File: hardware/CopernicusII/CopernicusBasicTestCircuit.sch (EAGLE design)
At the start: 6 parts, among them M1 COPERNICUS_II_MODULE

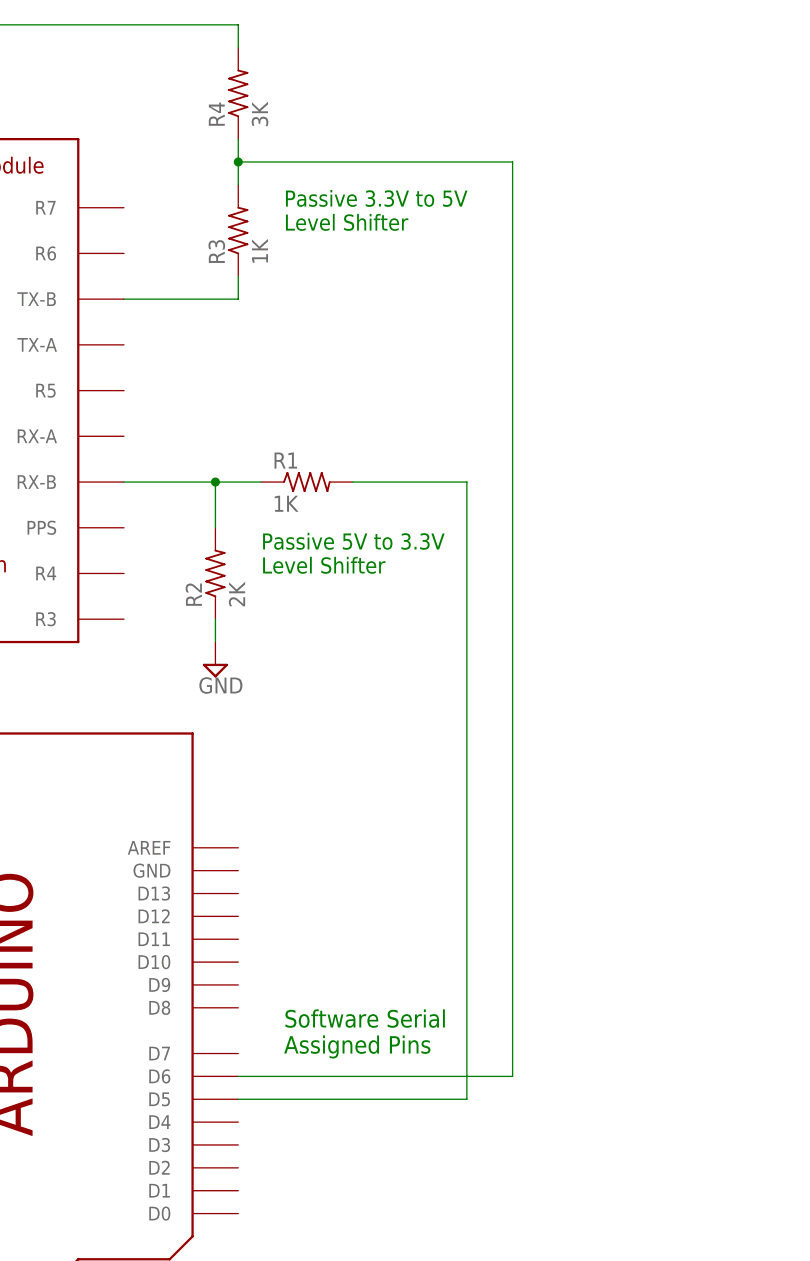
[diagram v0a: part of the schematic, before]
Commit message: Faster I/O with AltSoftSerial;Improved baud rate finding bug
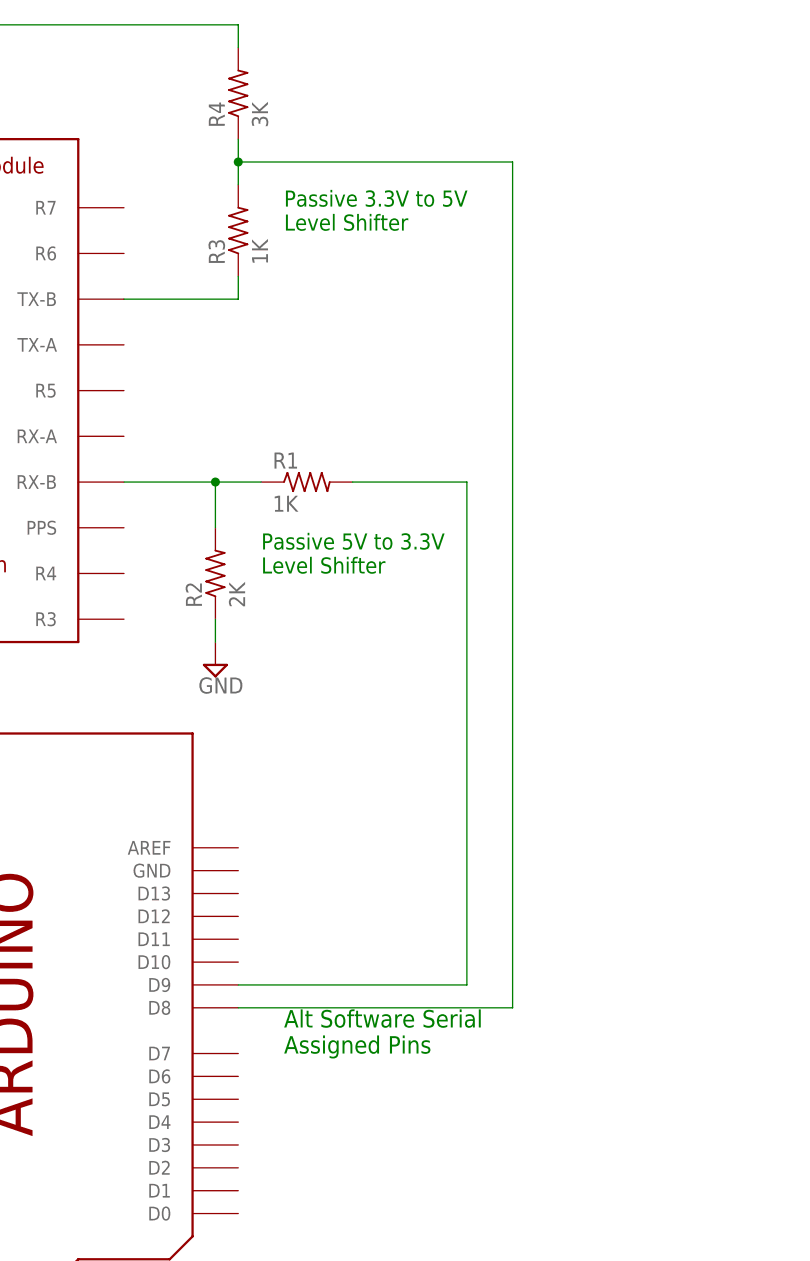
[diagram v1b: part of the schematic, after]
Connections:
- net N$2: now also U$1.D8; no longer U$1.D6
- net N$4: now also U$1.D9; no longer U$1.D5
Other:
- note added: "Alt Software Serial Assigned Pins"
- note removed: "Software Serial Assigned Pins"
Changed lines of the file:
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@@
 <plain>
 <text x="38.1" y="127" size="3.81" layer="91">Trimble Copernicus II Sparkfun Module Basic Test Circuit</text>
-<text x="144.78" y="7.62" size="1.9304" layer="91">Software Serial
+<text x="144.78" y="7.62" size="1.9304" layer="91">Alt Software Serial
 Assigned Pins</text>
 <text x="43.18" y="-12.7" size="1.778" layer="91">Rev 2.0.0
@@
 <pinref part="R1" gate="G$1" pin="2"/>
 <wire x1="165.1" y1="71.12" x2="152.4" y2="71.12" width="0.1524" layer="91"/>
-<wire x1="165.1" y1="71.12" x2="165.1" y2="2.54" width="0.1524" layer="91"/>
-<pinref part="U$1" gate="G$1" pin="D5"/>
-<wire x1="139.7" y1="2.54" x2="165.1" y2="2.54" width="0.1524" layer="91"/>
+<pinref part="U$1" gate="G$1" pin="D9"/>
+<wire x1="139.7" y1="15.24" x2="165.1" y2="15.24" width="0.1524" layer="91"/>
+<wire x1="165.1" y1="15.24" x2="165.1" y2="71.12" width="0.1524" layer="91"/>
 </segment>
 </net>
@@
 <net name="N$2" class="0">
 <segment>
-<wire x1="170.18" y1="106.68" x2="170.18" y2="5.08" width="0.1524" layer="91"/>
 <pinref part="R4" gate="G$1" pin="1"/>
 <pinref part="R3" gate="G$1" pin="2"/>
@@
 <wire x1="170.18" y1="106.68" x2="139.7" y2="106.68" width="0.1524" layer="91"/>
 <junction x="139.7" y="106.68"/>
-<pinref part="U$1" gate="G$1" pin="D6"/>
-<wire x1="139.7" y1="5.08" x2="170.18" y2="5.08" width="0.1524" layer="91"/>
+<pinref part="U$1" gate="G$1" pin="D8"/>
+<wire x1="139.7" y1="12.7" x2="170.18" y2="12.7" width="0.1524" layer="91"/>
+<wire x1="170.18" y1="12.7" x2="170.18" y2="106.68" width="0.1524" layer="91"/>
 </segment>
 </net>
